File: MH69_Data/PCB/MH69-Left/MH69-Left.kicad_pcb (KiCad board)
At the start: 2 copper layers, 164.5 x 97 mm, 77 parts, among them U1 nice_nano

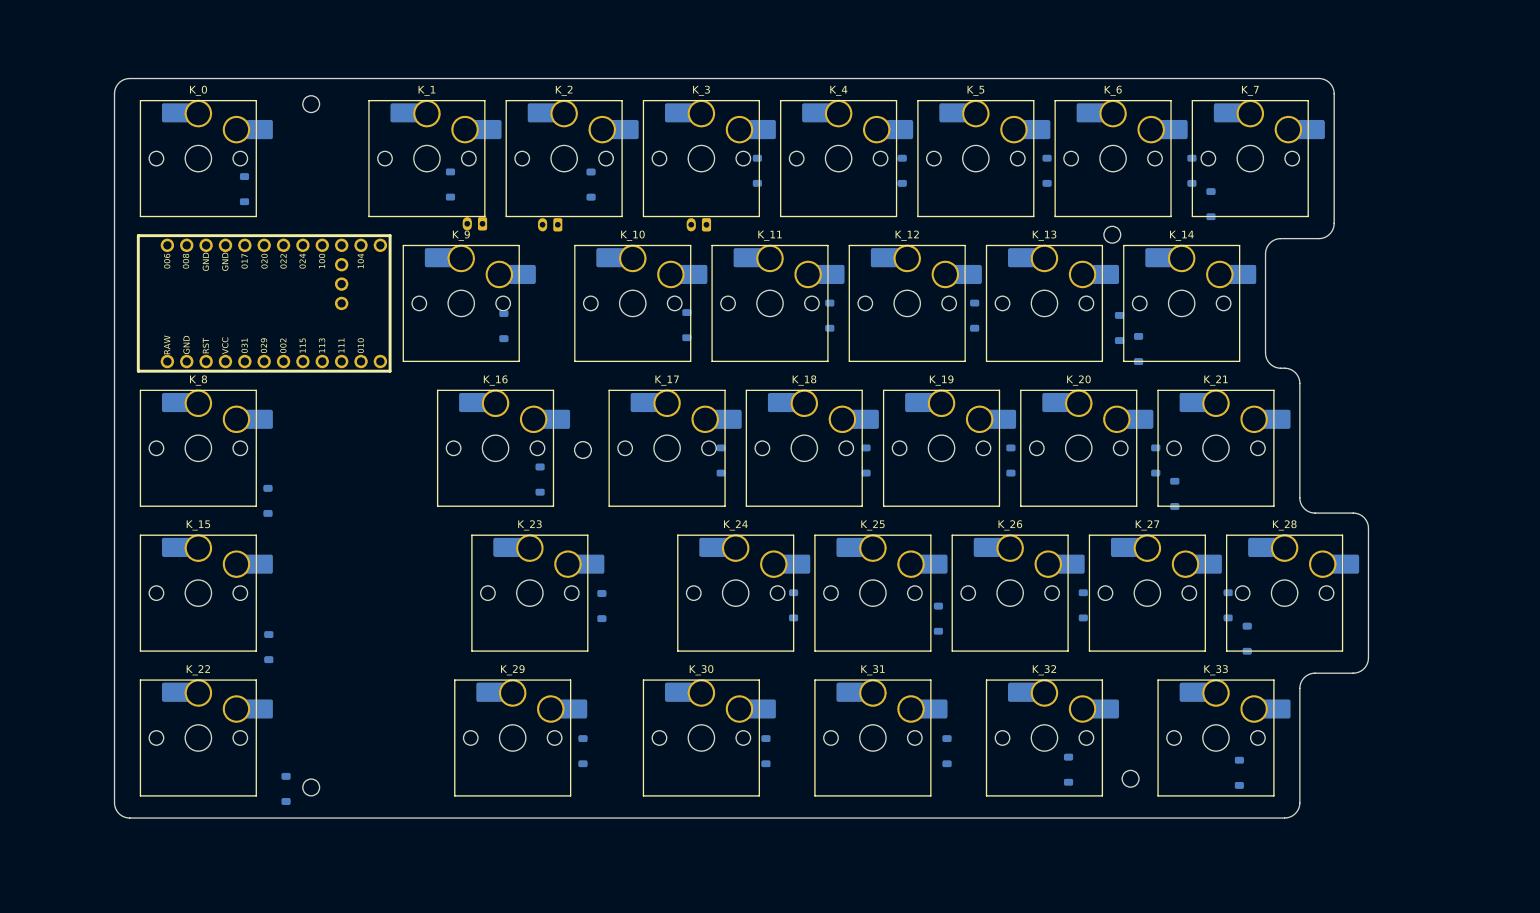
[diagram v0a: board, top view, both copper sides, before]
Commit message: updated diode locations
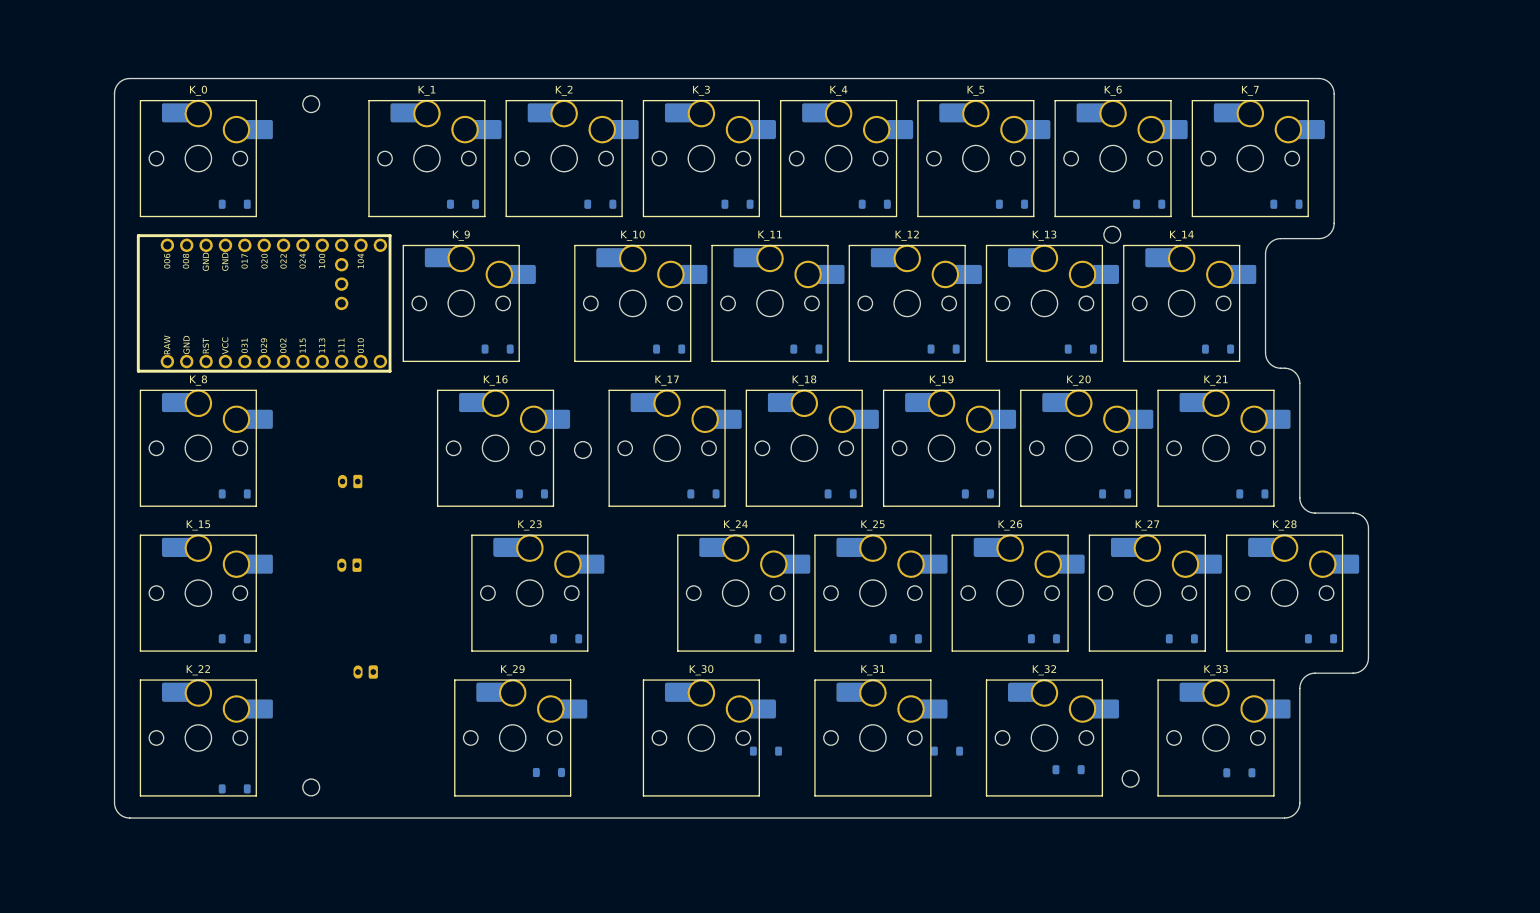
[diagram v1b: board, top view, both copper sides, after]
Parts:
- moved RST1 73.2 mm to (64.7, 129.1)
- moved PWR1 51.8 mm to (62.6, 115.1)
- moved Batt1 37.6 mm to (62.7, 104.1)
- moved D_14 10.4 mm to (175.6, 86.8), turned to 0 degrees
- moved D_21 10.2 mm to (180.1, 105.8), turned to 0 degrees
- moved D_7 9.90 mm to (184.5, 67.8), turned to 0 degrees
- moved D_28 9.68 mm to (189.1, 124.8), turned to 0 degrees
- moved D_27 7.49 mm to (170.8, 124.8), turned to 0 degrees
- moved D_6 7.12 mm to (166.5, 67.8), turned to 0 degrees
- moved D_20 6.90 mm to (162.1, 105.8), turned to 0 degrees
- moved D_26 6.78 mm to (152.7, 124.8), turned to 0 degrees
- moved D_22 6.73 mm to (46.6, 144.4), turned to 0 degrees
- moved D_5 6.36 mm to (148.5, 67.8), turned to 0 degrees
- moved D_23 6.35 mm to (90.0, 124.8), turned to 0 degrees
- moved D_19 6.16 mm to (144.1, 105.8), turned to 0 degrees
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
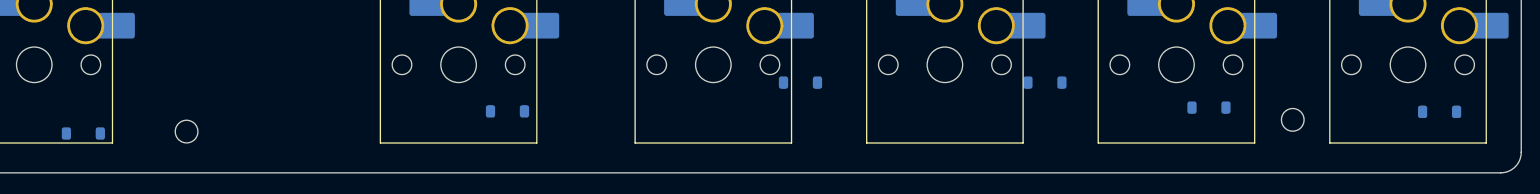
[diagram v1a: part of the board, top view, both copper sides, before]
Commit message: completed left side diode placement
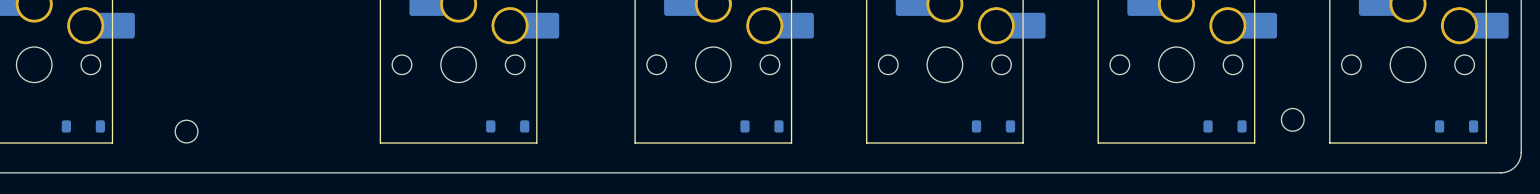
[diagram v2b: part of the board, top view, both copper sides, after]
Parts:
- moved D_31 6.57 mm to (135.0, 143.8)
- moved D_30 5.67 mm to (112.5, 143.8)
- moved D_32 2.41 mm to (157.5, 143.8)
- moved D_33 2.18 mm to (180.0, 143.8)
- moved D_29 1.46 mm to (87.8, 143.8)
- moved D_22 0.69 mm to (46.6, 143.8)

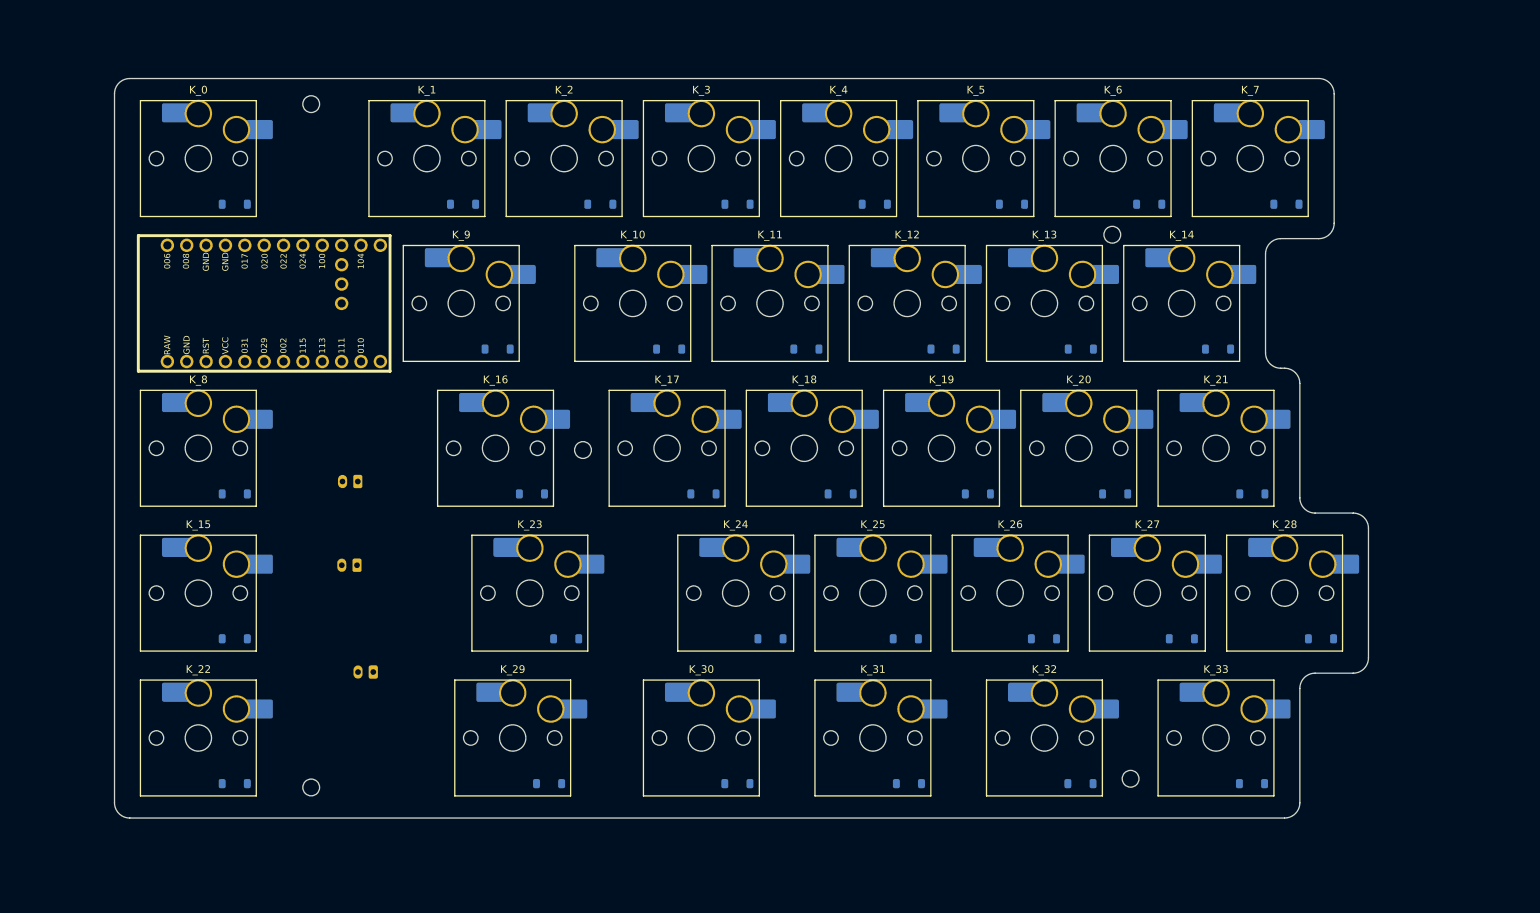
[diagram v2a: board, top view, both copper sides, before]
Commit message: started left routing
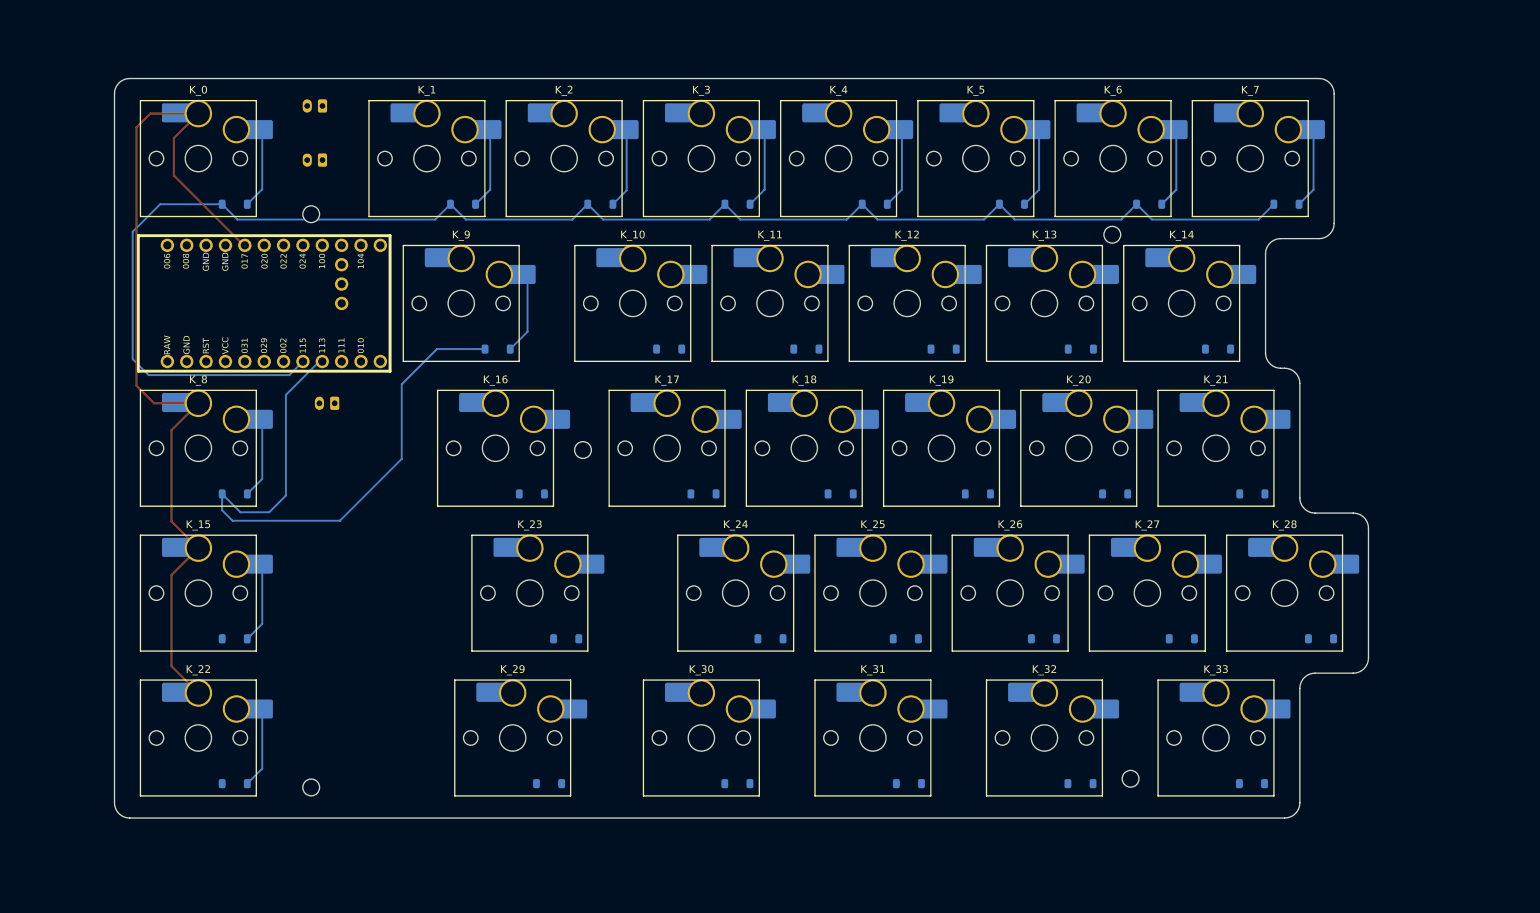
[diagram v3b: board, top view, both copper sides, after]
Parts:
- moved RST1 67.5 mm to (58.1, 62.0)
- moved PWR1 60.4 mm to (58.1, 54.9)
- moved H6 14.4 mm to (56.6, 69.1)
- moved Batt1 10.7 mm to (59.7, 93.9)
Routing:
- net row0: track 0.00 -> 203.5 mm
- net col0: track 0.00 -> 118.2 mm
- net row1: track 0.00 -> 82.3 mm
- net Net-(D_9-A): track 0.00 -> 11.1 mm
- net Net-(D_8-A): track 0.00 -> 10.8 mm
- net Net-(D_15-A): track 0.00 -> 10.8 mm
- net Net-(D_0-A): track 0.00 -> 10.8 mm
- net Net-(D_22-A): track 0.00 -> 10.8 mm
- net Net-(D_4-A): track 0.00 -> 10.8 mm
- net Net-(D_7-A): track 0.00 -> 10.8 mm
- net Net-(D_6-A): track 0.00 -> 10.8 mm
- net Net-(D_5-A): track 0.00 -> 10.8 mm
- net Net-(D_3-A): track 0.00 -> 10.8 mm
- net Net-(D_1-A): track 0.00 -> 10.8 mm
- net Net-(D_2-A): track 0.00 -> 10.7 mm

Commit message: completed all routing for left except power etc
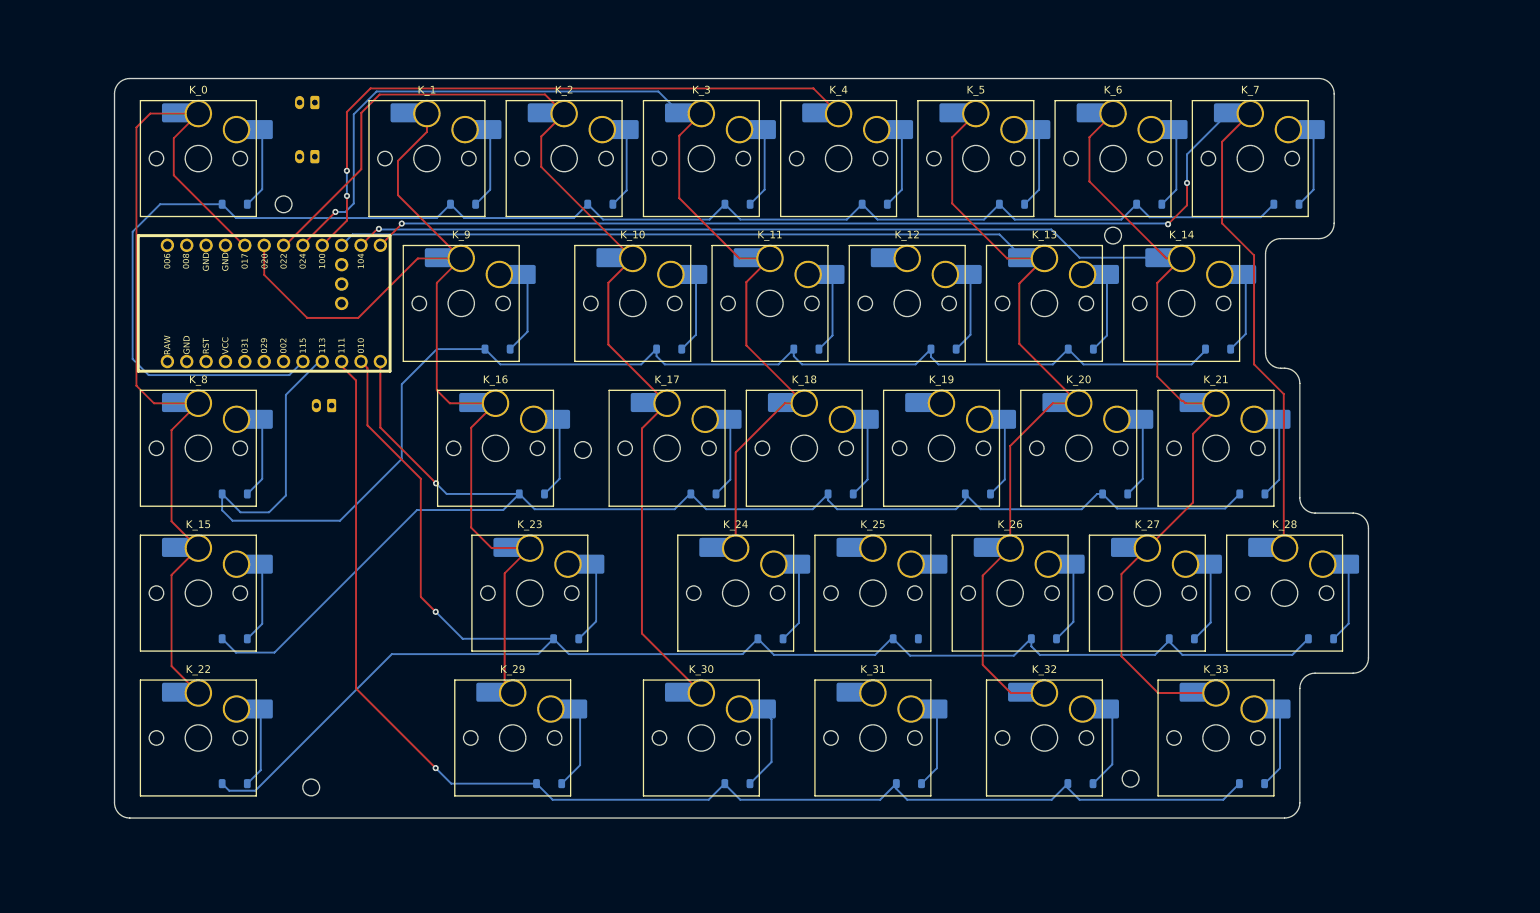
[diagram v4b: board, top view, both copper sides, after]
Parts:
- moved H6 3.85 mm to (53.0, 67.8)
- moved PWR1 1.10 mm to (57.1, 54.4)
- moved RST1 1.10 mm to (57.1, 61.5)
- moved Batt1 0.50 mm to (59.3, 94.2)
- moved H2 0.15 mm to (161.8, 71.9)
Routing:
- net row3: track 0.00 -> 214.6 mm, vias 0 -> 1
- net col6: track 0.00 -> 212.4 mm, vias 0 -> 1
- net col5: track 0.00 -> 194.1 mm
- net col7: track 0.00 -> 184.4 mm, vias 0 -> 3
- net row2: track 0.00 -> 182.5 mm, vias 0 -> 1
- net row4: track 0.00 -> 172.5 mm, vias 0 -> 1
- net col2: track 0.00 -> 141.7 mm
- net col3: track 0.00 -> 141.0 mm, vias 0 -> 1
- net col1: track 0.00 -> 133.6 mm
- net row1: track 82.3 -> 186.9 mm
- net col4: track 0.00 -> 86.0 mm, vias 0 -> 2
- net Net-(D_30-A): track 0.00 -> 11.5 mm
- net Net-(D_32-A): track 0.00 -> 11.3 mm
- net Net-(D_29-A): track 0.00 -> 11.2 mm
- net Net-(D_23-A): track 0.00 -> 11.1 mm
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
